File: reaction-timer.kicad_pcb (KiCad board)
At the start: 2 copper layers, 0 parts

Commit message: Add 48x80 mm board edges
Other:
- board outline added: 48 x 80 mm
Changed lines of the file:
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@@
     (area 0 0 0 0)
     (thickness 1.6)
-    (drawings 0)
+    (drawings 8)
     (tracks 0)
     (zones 0)
@@
     (uvia_drill 0.1)
   )
+  (gr_line (start 56 140) (end 56 70) (angle 90) (layer Edge.Cuts) (width 0.1))
+  (gr_line (start 104 140) (end 56 140) (angle 90) (layer Edge.Cuts) (width 0.1))
+  (gr_line (start 104 70) (end 104 140) (angle 90) (layer Edge.Cuts) (width 0.1))
+  (gr_arc (start 56 66) (end 60 66) (angle 90) (layer Edge.Cuts) (width 0.1))
+  (gr_line (start 60 60) (end 60 66) (angle 90) (layer Edge.Cuts) (width 0.1))
+  (gr_arc (start 104 66) (end 104 70) (angle 90) (layer Edge.Cuts) (width 0.1))
+  (gr_line (start 100 60) (end 100 66) (angle 90) (layer Edge.Cuts) (width 0.1))
+  (gr_line (start 60 60) (end 100 60) (angle 90) (layer Edge.Cuts) (width 0.1))
 )

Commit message: Read netlist
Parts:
- added AFF1, AFF2, AFF3: LTS-6980HR, Displays_7-Segment:7SegmentLED_LTS6760_LTS6780, F.Cu at (80.0, 150.1)
- added BT1: 9V_Battery, Pin_Headers:Pin_Header_Straight_1x02, F.Cu at (80.0, 150.1)
- added C1: CP, Capacitors_Elko_ThroughHole:Elko_vert_11x5mm_RM2.5, F.Cu at (80.0, 150.1)
- added C2, C3, C4, C6: C, Capacitors_ThroughHole:C_Disc_D7.5_P5, F.Cu at (80.0, 150.1)
- added C5: CP, Capacitors_Elko_ThroughHole:Elko_vert_11x5mm_RM2, F.Cu at (80.0, 150.1)
- added D1: D, Diodes_ThroughHole:Diode_DO-41_SOD81_Horizontal_RM10, F.Cu at (80.0, 150.1)
- added IC1, IC2, IC3: 4026, Housings_DIP:DIP-16_W7.62mm_LongPads, F.Cu at (80.0, 150.1)
- added IC5, IC6, IC7: NE555P, Housings_DIP:DIP-8_W7.62mm_LongPads, F.Cu at (80.0, 150.1)
- added LED1: LED, LEDs:LED-5MM, F.Cu at (80.0, 150.1)
- added R1, R10, R11, R12, R13, R14, R2, R3, R4, R5, R6, R7, R9: R, Resistors_ThroughHole:Resistor_Horizontal_RM10mm, F.Cu at (80.0, 150.1)
- added R8: POT, Potentiometers:Potentiometer_Bourns_3296W_3-8Zoll_Inline_ScrewUp, F.Cu at (80.0, 150.1)
- added S2: SET_TO_ZERO, Pin_Headers:Pin_Header_Straight_1x02, F.Cu at (80.0, 150.1)
- added S3: STOP, Pin_Headers:Pin_Header_Straight_1x02, F.Cu at (80.0, 150.1)
- added S4: START_DELAY, Pin_Headers:Pin_Header_Straight_1x02, F.Cu at (80.0, 150.1)

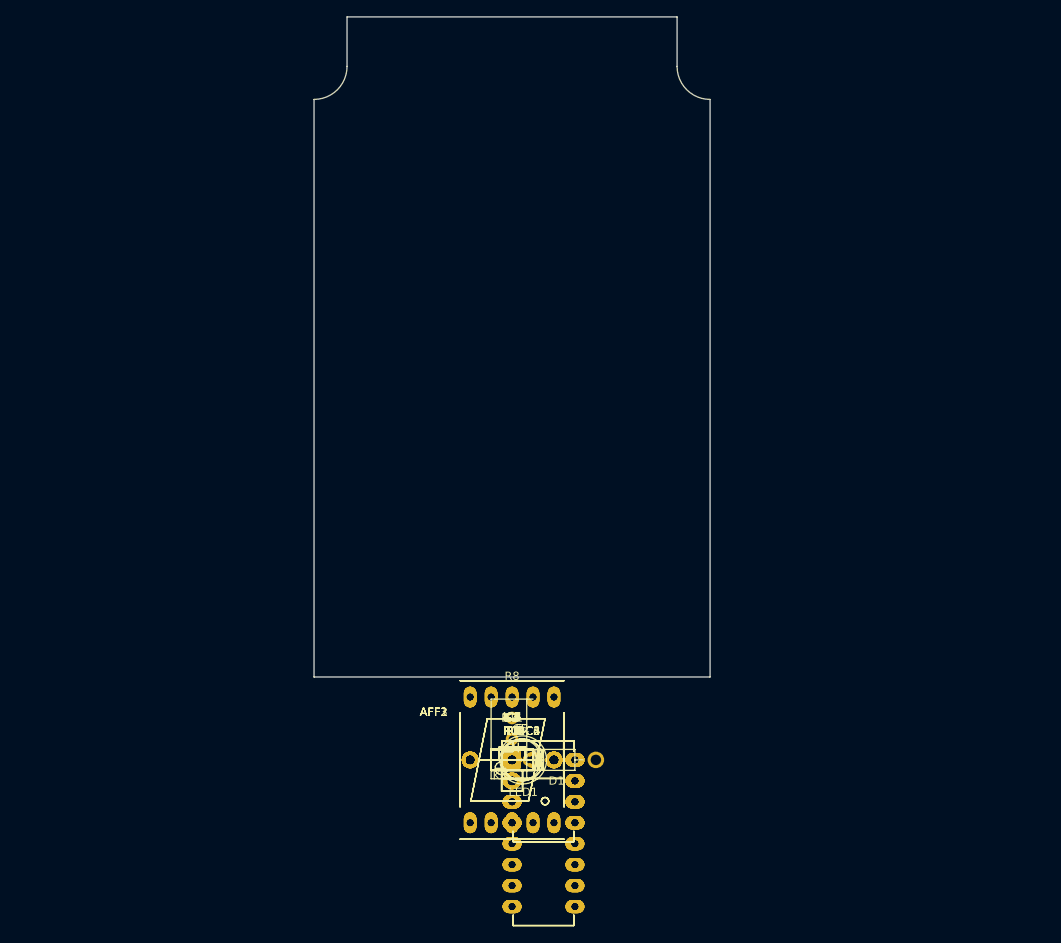
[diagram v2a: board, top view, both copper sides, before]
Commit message: Start placing footprints on board
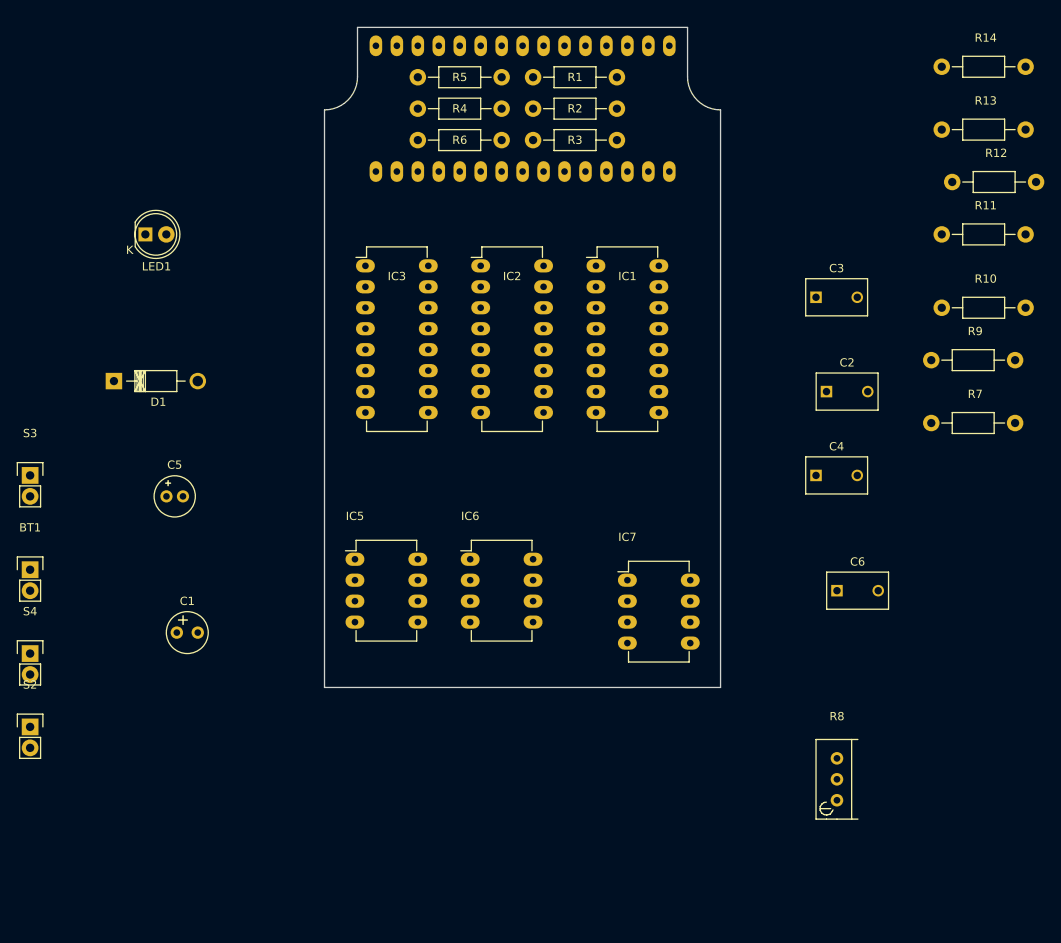
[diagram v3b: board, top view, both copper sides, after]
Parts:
- AFF1, AFF2, AFF3: moved to B.Cu
- moved R14 101.6 mm to (137.2, 66.0)
- moved R13 95.4 mm to (137.2, 73.7)
- moved R12 91.2 mm to (138.4, 80.0)
- moved R11 85.6 mm to (137.2, 86.4)
- moved R1 83.1 mm to (87.6, 67.3)
- moved R5 83.0 mm to (73.7, 67.3), turned to 180 degrees
- moved AFF1 80.2 mm to (94.0, 71.1), turned to 180 degrees
- moved AFF3 79.8 mm to (68.6, 71.1), turned to 180 degrees
- moved R2 79.3 mm to (87.6, 71.1)
- moved R10 79.2 mm to (137.2, 95.2)
- moved R4 79.2 mm to (73.7, 71.1)
- moved AFF2 78.9 mm to (81.3, 71.1), turned to 180 degrees
- moved LED1 77.7 mm to (35.6, 86.4)
- moved R3 75.5 mm to (87.6, 74.9), turned to 180 degrees
- moved R6 75.4 mm to (73.7, 74.9), turned to 180 degrees
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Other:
- net class Default: clearance 0.2 -> 0.17; trace_width 0.25 -> 0.2
- net class Power added: clearance 0.2, trace_width 0.3, via_dia 0.6, via_drill 0.4
- rule trace_clearance: 0.2 -> 0.17
- rule trace_min: 0.2 -> 0.16

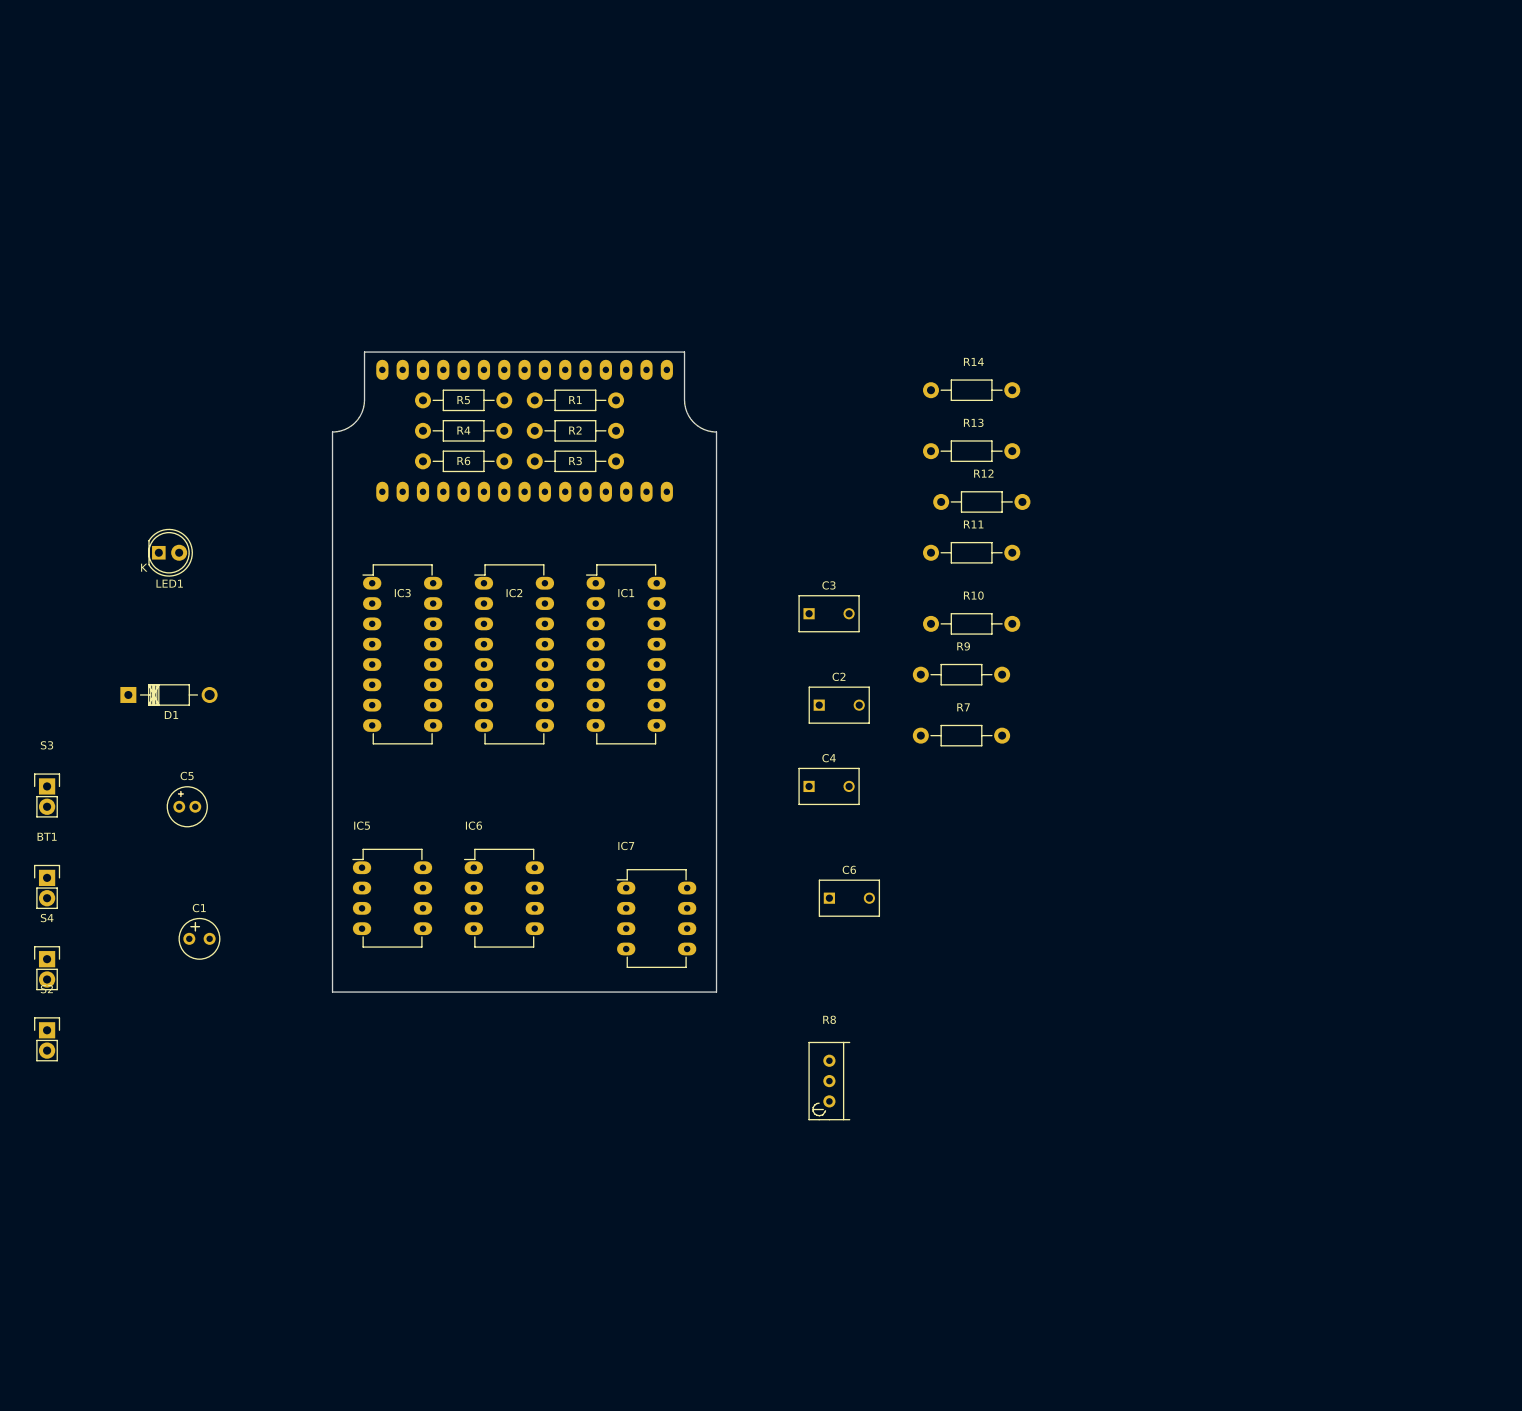
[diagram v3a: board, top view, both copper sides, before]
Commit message: Add mounting holes to PCB
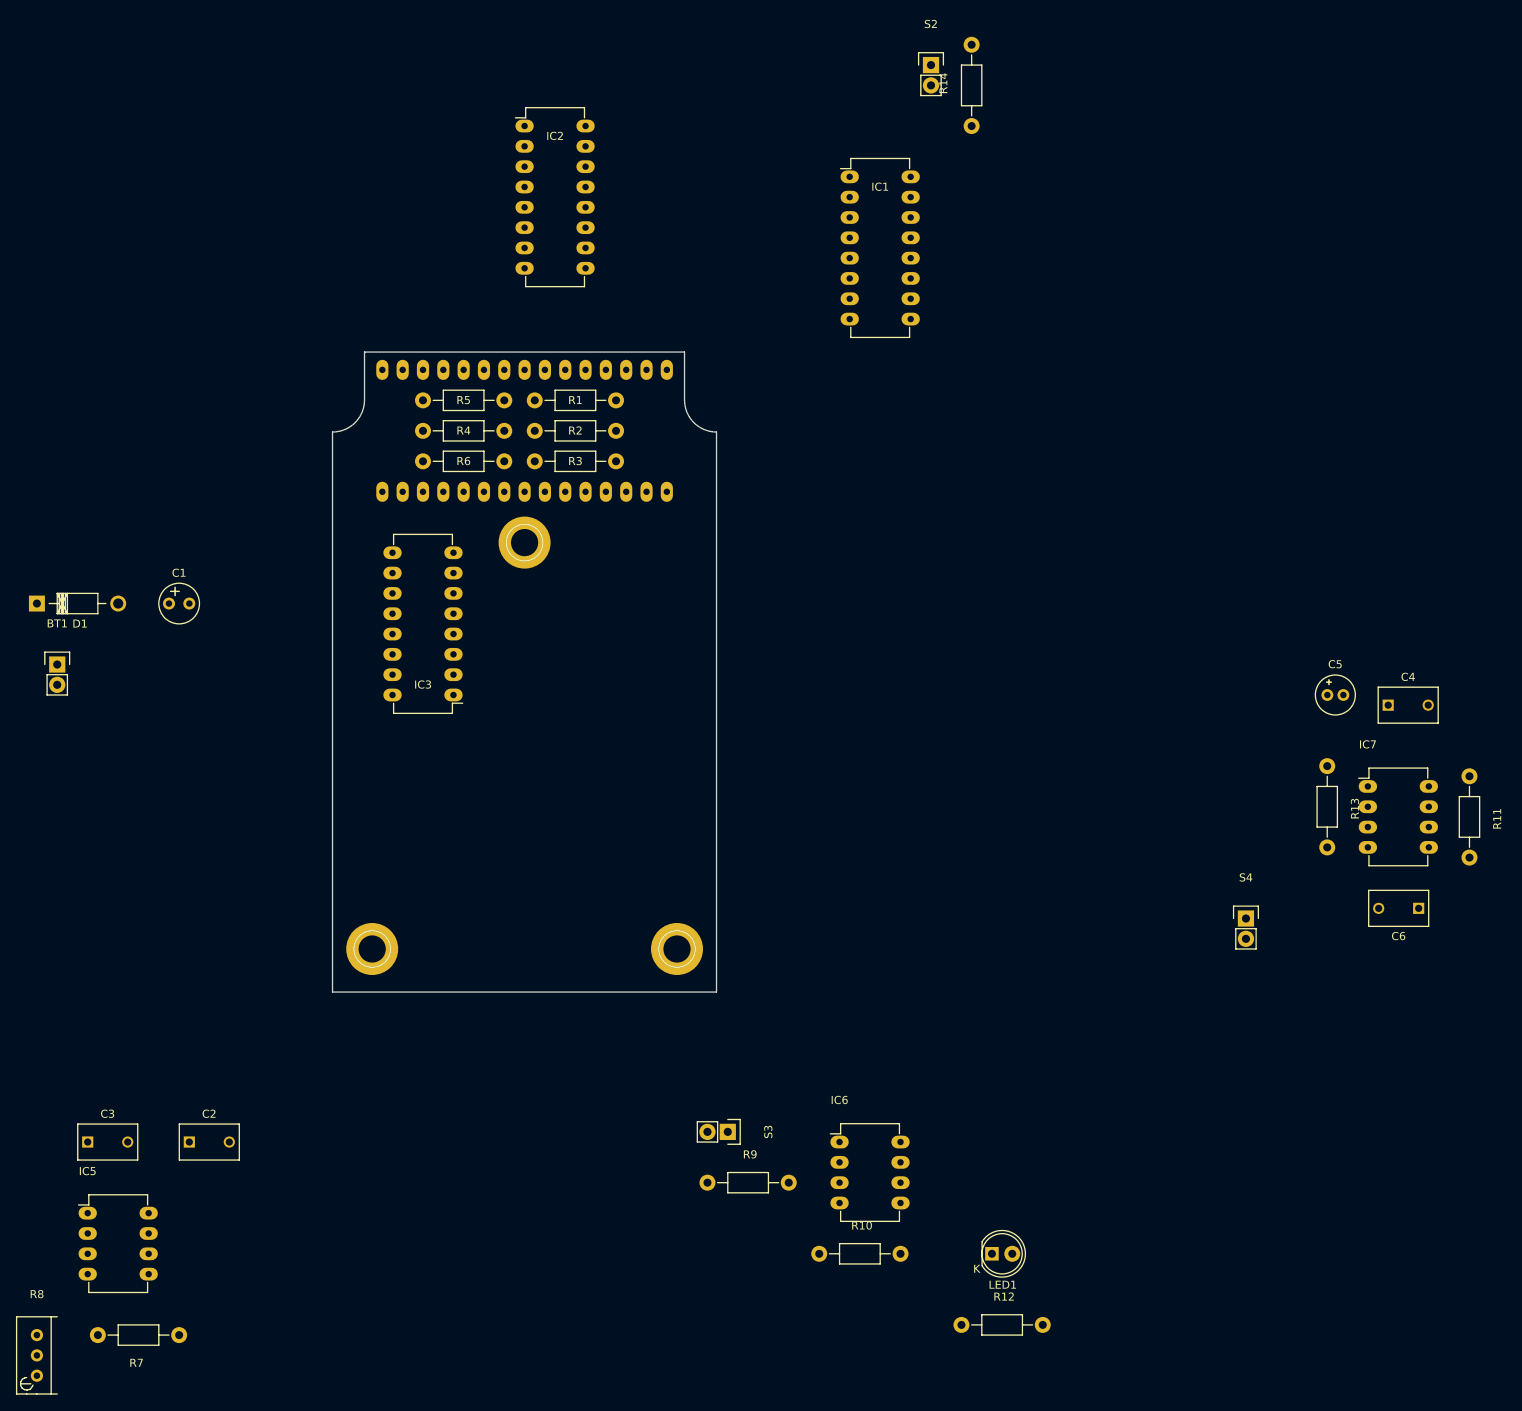
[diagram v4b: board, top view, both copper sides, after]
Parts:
- added REF**: 1pin, Connect:1pin, F.Cu at (62.2, 135.9)
- added REF**: 1pin, Connect:1pin, F.Cu at (100.3, 135.9)
- added REF**: 1pin, Connect:1pin, F.Cu at (81.3, 85.1)
- moved S2 163.6 mm to (132.1, 25.4)
- moved S4 149.9 mm to (171.4, 132.1)
- moved C5 144.2 mm to (181.6, 104.1)
- moved LED1 136.1 mm to (139.7, 174.0)
- moved R7 127.3 mm to (33.0, 184.2), turned to 180 degrees
- moved C3 111.8 mm to (26.7, 160.0)
- moved R8 104.8 mm to (20.3, 189.2)
- moved R12 102.9 mm to (141.0, 182.9)
- moved C2 95.8 mm to (39.4, 160.0)
- moved S3 95.4 mm to (106.7, 158.8), turned to 270 degrees
- moved IC7 93.6 mm to (186.7, 115.6)
- moved R10 80.0 mm to (123.2, 174.0)
- moved C6 73.7 mm to (193.0, 130.8), turned to 180 degrees
- moved C4 73.1 mm to (189.2, 105.4)
- moved R11 70.4 mm to (199.4, 119.4), turned to 270 degrees
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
